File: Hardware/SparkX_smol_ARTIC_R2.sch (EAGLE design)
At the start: 117 parts, among them J25 U.FL, K1 TLP3475SRHA, Q2 5.8A/30V/35mΩ, U1 ADM4210_1TSOT6, U2 1.8V/100mA, U3 ARTIC_R2, U4 RFPA0133, U5 AS179-92LF, U6 3.0V, U7 SST25VF020BUSON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

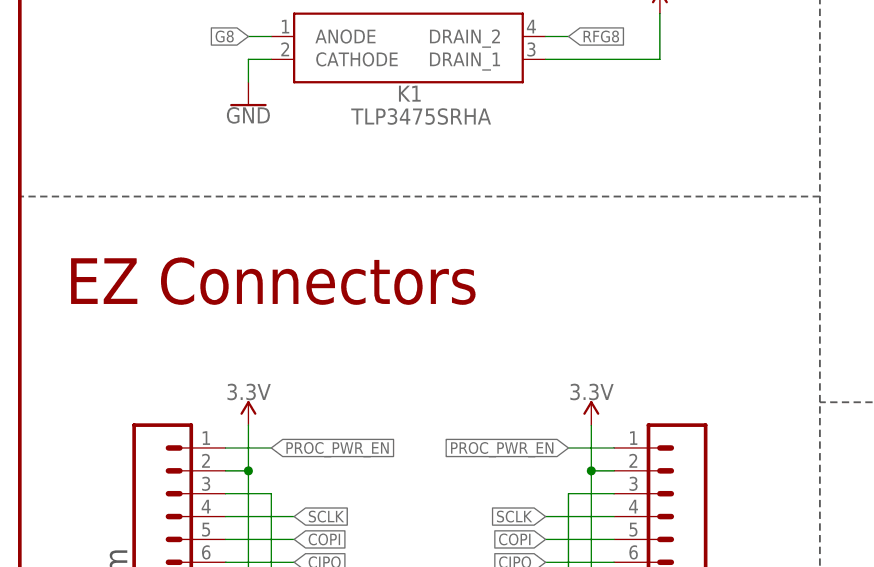
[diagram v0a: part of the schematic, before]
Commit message: Change EZ to smôl on schematic
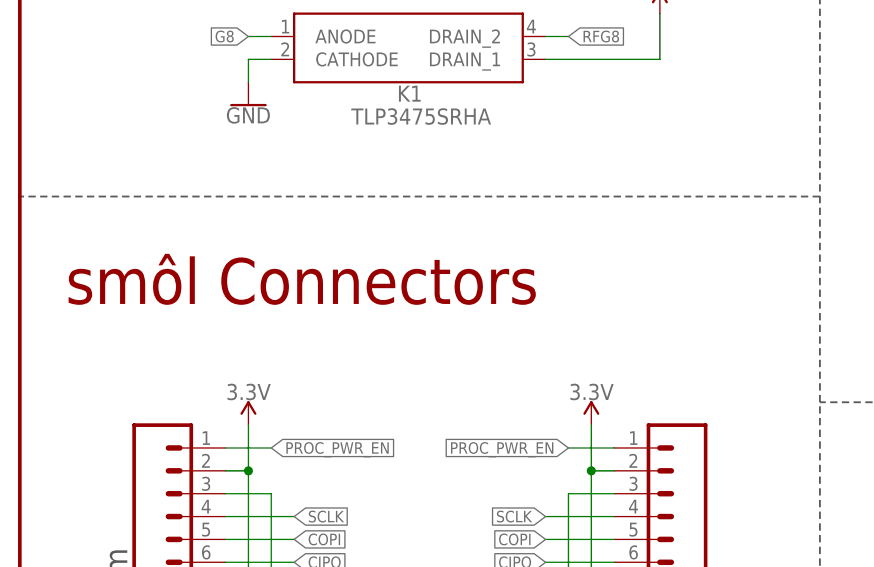
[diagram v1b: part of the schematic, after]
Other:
- note added: "smôl Connectors"
- note removed: "EZ Connectors"
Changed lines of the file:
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@@
 <wire x1="88.9" y1="167.64" x2="0" y2="167.64" width="0.2032" layer="97" style="longdash"/>
 <text x="5.08" y="157.48" size="5.08" layer="94">FLASH Memory</text>
-<text x="5.08" y="66.802" size="5.08" layer="94">EZ Connectors</text>
+<text x="5.08" y="66.802" size="5.08" layer="94">smôl Connectors</text>
 <text x="11.938" y="28.194" size="2.54" layer="97" font="vector" rot="R90">Bottom</text>
 <text x="76.962" y="35.56" size="2.54" layer="97" font="vector" rot="R270">Top</text>

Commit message: Change ADM4210-1 from IC-16020 to IC-14694
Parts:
- L1, L10, L13, L14, L15, L2, L3, L4, L9: device SparkFun-Coils:FERRITE_BEAD-0402-30OHM-100MHZ -> SparkFun-Coils:FERRITE_BEAD-0402-30Ω-100MHZ
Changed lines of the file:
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@@
 <layer number="154" name="FabDoc2" color="7" fill="1" visible="no" active="no"/>
 <layer number="155" name="FabDoc3" color="7" fill="1" visible="no" active="no"/>
+<layer number="156" name="gesam-Maß" color="1" fill="7" visible="no" active="no"/>
+<layer number="157" name="FaceMchng" color="3" fill="1" visible="no" active="no"/>
+<layer number="158" name="FaceMMeas" color="3" fill="1" visible="no" active="no"/>
+<layer number="159" name="Geh-Bear2" color="1" fill="7" visible="no" active="no"/>
+<layer number="160" name="Topologie" color="9" fill="1" visible="no" active="no"/>
+<layer number="161" name="tomplace2" color="7" fill="1" visible="no" active="no"/>
 <layer number="166" name="AntennaArea" color="7" fill="1" visible="no" active="no"/>
 <layer number="168" name="4mmHeightArea" color="7" fill="1" visible="no" active="no"/>
@@
 <layer number="250" name="Descript" color="3" fill="1" visible="no" active="no"/>
 <layer number="251" name="SMDround" color="12" fill="11" visible="no" active="no"/>
+<layer number="252" name="BR-BS" color="7" fill="1" visible="no" active="no"/>
 <layer number="253" name="Extra" color="7" fill="1" visible="no" active="no"/>
 <layer number="254" name="cooling" color="7" fill="1" visible="no" active="no"/>
@@
 <part name="GND8" library="SparkFun-PowerSymbols" deviceset="GND" device=""/>
 <part name="GND9" library="SparkFun-PowerSymbols" deviceset="GND" device=""/>
-<part name="L13" library="SparkFun-Coils" deviceset="FERRITE_BEAD" device="-0402-30OHM-100MHZ" value="30Ω"/>
+<part name="L13" library="SparkFun-Coils" deviceset="FERRITE_BEAD" device="-0402-30Ω-100MHZ" value="30Ω"/>
 <part name="C34" library="SparkFun-Capacitors" deviceset="22PF" device="-0402T-16V-10%" value="22pF"/>
 <part name="C35" library="SparkFun-Capacitors" deviceset="0.1UF" device="-0402T-6.3V-10%-X7R" value="0.1uF"/>
@@
 <part name="GND11" library="SparkFun-PowerSymbols" deviceset="GND" device=""/>
 <part name="SUPPLY8" library="SparkFun-PowerSymbols" deviceset="VDD" device=""/>
-<part name="L15" library="SparkFun-Coils" deviceset="FERRITE_BEAD" device="-0402-30OHM-100MHZ" value="30Ω"/>
+<part name="L15" library="SparkFun-Coils" deviceset="FERRITE_BEAD" device="-0402-30Ω-100MHZ" value="30Ω"/>
 <part name="C40" library="SparkFun-Capacitors" deviceset="22PF" device="-0402T-16V-10%" value="22pF"/>
 <part name="C41" library="SparkFun-Capacitors" deviceset="0.1UF" device="-0402T-6.3V-10%-X7R" value="0.1uF"/>
@@
 <part name="GND13" library="SparkFun-PowerSymbols" deviceset="GND" device=""/>
 <part name="SUPPLY5" library="SparkFun-PowerSymbols" deviceset="1.8V" device=""/>
-<part name="L9" library="SparkFun-Coils" deviceset="FERRITE_BEAD" device="-0402-30OHM-100MHZ" value="30Ω"/>
+<part name="L9" library="SparkFun-Coils" deviceset="FERRITE_BEAD" device="-0402-30Ω-100MHZ" value="30Ω"/>
 <part name="C27" library="SparkFun-Capacitors" deviceset="22PF" device="-0402T-16V-10%" value="22pF"/>
 <part name="C26" library="SparkFun-Capacitors" deviceset="0.1UF" device="-0402T-6.3V-10%-X7R" value="0.1uF"/>
@@
 <part name="GND17" library="SparkFun-PowerSymbols" deviceset="GND" device=""/>
 <part name="SUPPLY9" library="SparkFun-PowerSymbols" deviceset="VDD" device=""/>
-<part name="L10" library="SparkFun-Coils" deviceset="FERRITE_BEAD" device="-0402-30OHM-100MHZ" value="30Ω"/>
+<part name="L10" library="SparkFun-Coils" deviceset="FERRITE_BEAD" device="-0402-30Ω-100MHZ" value="30Ω"/>
 <part name="C33" library="SparkFun-Capacitors" deviceset="22PF" device="-0402T-16V-10%" value="22pF"/>
 <part name="C32" library="SparkFun-Capacitors" deviceset="0.1UF" device="-0402T-6.3V-10%-X7R" value="0.1uF"/>
@@
 <part name="R8" library="SparkFun-Resistors" deviceset="100KOHM" device="-0402T-1/16W-1%" value="100k"/>
 <part name="R5" library="SparkFun-Resistors" deviceset="100KOHM" device="-0402T-1/16W-1%" value="100k"/>
-<part name="L4" library="SparkFun-Coils" deviceset="FERRITE_BEAD" device="-0402-30OHM-100MHZ" value="30Ω"/>
+<part name="L4" library="SparkFun-Coils" deviceset="FERRITE_BEAD" device="-0402-30Ω-100MHZ" value="30Ω"/>
 <part name="GND20" library="SparkFun-PowerSymbols" deviceset="GND" device=""/>
 <part name="GND21" library="SparkFun-PowerSymbols" deviceset="GND" device=""/>
 <part name="SUPPLY11" library="SparkFun-PowerSymbols" deviceset="VDD" device=""/>
-<part name="L3" library="SparkFun-Coils" deviceset="FERRITE_BEAD" device="-0402-30OHM-100MHZ" value="30Ω"/>
+<part name="L3" library="SparkFun-Coils" deviceset="FERRITE_BEAD" device="-0402-30Ω-100MHZ" value="30Ω"/>
 <part name="C7" library="SparkFun-Capacitors" deviceset="22PF" device="-0402T-16V-10%" value="22pF"/>
 <part name="C8" library="SparkFun-Capacitors" deviceset="0.1UF" device="-0402T-6.3V-10%-X7R" value="0.1uF"/>
@@
 <part name="R4" library="SparkFun-Resistors" deviceset="33KOHM" device="-0402T-1/16W-1%" value="33k"/>
 <part name="GND24" library="SparkFun-PowerSymbols" deviceset="GND" device=""/>
-<part name="L2" library="SparkFun-Coils" deviceset="FERRITE_BEAD" device="-0402-30OHM-100MHZ" value="30Ω"/>
+<part name="L2" library="SparkFun-Coils" deviceset="FERRITE_BEAD" device="-0402-30Ω-100MHZ" value="30Ω"/>
 <part name="C5" library="SparkFun-Capacitors" deviceset="22PF" device="-0402T-16V-10%" value="22pF"/>
 <part name="C6" library="SparkFun-Capacitors" deviceset="0.1UF" device="-0402T-6.3V-10%-X7R" value="0.1uF"/>
@@
 <part name="GND47" library="SparkFun-PowerSymbols" deviceset="GND" device=""/>
 <part name="R3" library="SparkFun-Resistors" deviceset="3.9OHM" device="-0402-TIGHT-1/16W-1%" value="3.9"/>
-<part name="L14" library="SparkFun-Coils" deviceset="FERRITE_BEAD" device="-0402-30OHM-100MHZ" value="30Ω"/>
+<part name="L14" library="SparkFun-Coils" deviceset="FERRITE_BEAD" device="-0402-30Ω-100MHZ" value="30Ω"/>
 <part name="C39" library="SparkFun-Capacitors" deviceset="22PF" device="-0402T-16V-10%" value="22pF"/>
 <part name="C38" library="SparkFun-Capacitors" deviceset="0.1UF" device="-0402T-6.3V-10%-X7R" value="0.1uF"/>
@@
 <part name="U7" library="SparkFun-IC-Memory" deviceset="SST25VF020B" device="USON"/>
 <part name="GND53" library="SparkFun-PowerSymbols" deviceset="GND" device=""/>
-<part name="L1" library="SparkFun-Coils" deviceset="FERRITE_BEAD" device="-0402-30OHM-100MHZ" value="30Ω"/>
+<part name="L1" library="SparkFun-Coils" deviceset="FERRITE_BEAD" device="-0402-30Ω-100MHZ" value="30Ω"/>
 <part name="C50" library="SparkFun-Capacitors" deviceset="0.1UF" device="-0402T-6.3V-10%-X7R" value="0.1uF"/>
 <part name="GND55" library="SparkFun-PowerSymbols" deviceset="GND" device=""/>
@@
 <attribute name="VALUE" x="271.78" y="164.846" size="1.778" layer="96" font="vector" rot="MR0" align="top-center"/>
 </instance>
-<instance part="C17" gate="G$1" x="269.24" y="142.24" smashed="yes" rot="R270">
+<instance part="C17" gate="C1" x="269.24" y="142.24" smashed="yes" rot="R270">
 <attribute name="NAME" x="272.161" y="140.716" size="1.778" layer="95" font="vector" rot="R270"/>
 <attribute name="VALUE" x="267.081" y="140.716" size="1.778" layer="96" font="vector" rot="R270"/>
@@
 <wire x1="281.94" y1="157.48" x2="289.56" y2="157.48" width="0.1524" layer="91"/>
 <wire x1="289.56" y1="157.48" x2="289.56" y2="142.24" width="0.1524" layer="91"/>
-<pinref part="C17" gate="G$1" pin="1"/>
+<pinref part="C17" gate="C1" pin="1"/>
 <wire x1="289.56" y1="142.24" x2="274.32" y2="142.24" width="0.1524" layer="91"/>
 </segment>
@@
 <net name="N$16" class="0">
 <segment>
-<pinref part="C17" gate="G$1" pin="2"/>
+<pinref part="C17" gate="C1" pin="2"/>
 <wire x1="266.7" y1="142.24" x2="251.46" y2="142.24" width="0.1524" layer="91"/>
 <pinref part="U3" gate="G$1" pin="FREF"/>
